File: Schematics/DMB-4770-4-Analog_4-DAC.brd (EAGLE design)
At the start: 32.8 x 86.9 mm, 66 parts

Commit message: Ajout schemas pour carte 4 entrées analog et 4 sorties analog
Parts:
- E$42, E$44, E$47, E$48: value 100K -> 80K
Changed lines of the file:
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@@
 <attribute name="NAME" x="13.6525" y="10.795" size="1.27" layer="51" ratio="16" rot="R180"/>
 </element>
-<element name="E$42" library="divers" package="R0805" value="100K" x="11.7475" y="14.2875" smashed="yes">
+<element name="E$42" library="divers" package="R0805" value="80K" x="11.7475" y="14.2875" smashed="yes">
 <attribute name="VALUE" x="6.985" y="13.97" size="0.8128" layer="27" ratio="16"/>
 <attribute name="NAME" x="10.16" y="15.24" size="1.27" layer="25" ratio="16"/>
@@
 <attribute name="NAME" x="19.3675" y="12.3825" size="1.27" layer="51" ratio="16" rot="R180"/>
 </element>
-<element name="E$44" library="divers" package="R0805" value="100K" x="21.2725" y="13.97" smashed="yes">
+<element name="E$44" library="divers" package="R0805" value="80K" x="21.2725" y="13.97" smashed="yes">
 <attribute name="VALUE" x="20.0025" y="12.065" size="0.8128" layer="27" ratio="16"/>
 <attribute name="NAME" x="19.685" y="14.9225" size="1.27" layer="25" ratio="16"/>
@@
 <attribute name="NAME" x="18.0975" y="26.9875" size="1.27" layer="51" ratio="16"/>
 </element>
-<element name="E$47" library="divers" package="R0805" value="100K" x="23.8125" y="25.4" smashed="yes">
+<element name="E$47" library="divers" package="R0805" value="80K" x="23.8125" y="25.4" smashed="yes">
 <attribute name="VALUE" x="22.5425" y="26.3525" size="0.8128" layer="27" ratio="16"/>
 <attribute name="NAME" x="22.225" y="26.3525" size="1.27" layer="25" ratio="16"/>
 <attribute name="NAME" x="21.9075" y="26.9875" size="1.27" layer="51" ratio="16"/>
 </element>
-<element name="E$48" library="divers" package="R0805" value="100K" x="11.7475" y="25.4" smashed="yes">
+<element name="E$48" library="divers" package="R0805" value="80K" x="11.7475" y="25.4" smashed="yes">
 <attribute name="VALUE" x="10.4775" y="26.3525" size="0.8128" layer="27" ratio="16"/>
 <attribute name="NAME" x="10.16" y="26.3525" size="1.27" layer="25" ratio="16"/>

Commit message: Correction valeurs
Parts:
- E$11, E$12, E$14, E$15, E$27, E$28, E$33, E$34: value 120K -> 102K
- E$41, E$43, E$45, E$46: value 20K -> 82.5K
- E$42, E$44, E$47, E$48: value 80K -> 330K
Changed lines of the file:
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@@
 <attribute name="NAME" x="26.8288" y="48.1806" size="1.27" layer="51" ratio="16" rot="R270"/>
 </element>
-<element name="E$11" library="divers" package="R0805" value="120K" x="27.305" y="50.165" smashed="yes" rot="R90">
+<element name="E$11" library="divers" package="R0805" value="102K" x="27.305" y="50.165" smashed="yes" rot="R90">
 <attribute name="VALUE" x="27.6225" y="52.07" size="0.8128" layer="27" ratio="16" rot="R90"/>
 <attribute name="NAME" x="26.3525" y="48.5775" size="1.27" layer="25" ratio="16" rot="R90"/>
 <attribute name="NAME" x="25.7175" y="48.26" size="1.27" layer="51" ratio="16" rot="R90"/>
 </element>
-<element name="E$12" library="divers" package="R0805" value="120K" x="27.305" y="46.0375" smashed="yes" rot="R270">
+<element name="E$12" library="divers" package="R0805" value="102K" x="27.305" y="46.0375" smashed="yes" rot="R270">
 <attribute name="VALUE" x="26.9875" y="44.1325" size="0.8128" layer="27" ratio="16" rot="R270"/>
 <attribute name="NAME" x="28.2575" y="47.625" size="1.27" layer="25" ratio="16" rot="R270"/>
@@
 <attribute name="NAME" x="22.6219" y="60.4838" size="1.27" layer="51" ratio="16"/>
 </element>
-<element name="E$14" library="divers" package="R0805" value="120K" x="20.6375" y="60.96" smashed="yes" rot="R180">
+<element name="E$14" library="divers" package="R0805" value="102K" x="20.6375" y="60.96" smashed="yes" rot="R180">
 <attribute name="VALUE" x="21.9075" y="62.865" size="0.8128" layer="27" ratio="16" rot="R180"/>
 <attribute name="NAME" x="22.225" y="60.0075" size="1.27" layer="25" ratio="16" rot="R180"/>
 <attribute name="NAME" x="22.5425" y="59.3725" size="1.27" layer="51" ratio="16" rot="R180"/>
 </element>
-<element name="E$15" library="divers" package="R0805" value="120K" x="24.765" y="60.96" smashed="yes">
+<element name="E$15" library="divers" package="R0805" value="102K" x="24.765" y="60.96" smashed="yes">
 <attribute name="VALUE" x="23.8125" y="61.9125" size="0.8128" layer="27" ratio="16"/>
 <attribute name="NAME" x="23.1775" y="61.9125" size="1.27" layer="25" ratio="16"/>
@@
 <attribute name="NAME" x="10.2394" y="60.4838" size="1.27" layer="51" ratio="16"/>
 </element>
-<element name="E$27" library="divers" package="R0805" value="120K" x="8.255" y="60.96" smashed="yes" rot="R180">
+<element name="E$27" library="divers" package="R0805" value="102K" x="8.255" y="60.96" smashed="yes" rot="R180">
 <attribute name="VALUE" x="9.8425" y="62.865" size="0.8128" layer="27" ratio="16" rot="R180"/>
 <attribute name="NAME" x="9.8425" y="60.0075" size="1.27" layer="25" ratio="16" rot="R180"/>
 <attribute name="NAME" x="10.16" y="59.3725" size="1.27" layer="51" ratio="16" rot="R180"/>
 </element>
-<element name="E$28" library="divers" package="R0805" value="120K" x="12.3825" y="60.96" smashed="yes">
+<element name="E$28" library="divers" package="R0805" value="102K" x="12.3825" y="60.96" smashed="yes">
 <attribute name="VALUE" x="13.97" y="62.865" size="0.8128" layer="27" ratio="16" rot="R180"/>
 <attribute name="NAME" x="10.795" y="61.9125" size="1.27" layer="25" ratio="16"/>
@@
 <attribute name="NAME" x="5.8737" y="48.0219" size="1.27" layer="51" ratio="16" rot="R90"/>
 </element>
-<element name="E$33" library="divers" package="R0805" value="120K" x="4.7625" y="46.0375" smashed="yes" rot="R270">
+<element name="E$33" library="divers" package="R0805" value="102K" x="4.7625" y="46.0375" smashed="yes" rot="R270">
 <attribute name="VALUE" x="4.445" y="44.1325" size="0.8128" layer="27" ratio="16" rot="R270"/>
 <attribute name="NAME" x="5.715" y="47.625" size="1.27" layer="25" ratio="16" rot="R270"/>
 <attribute name="NAME" x="6.35" y="47.9425" size="1.27" layer="51" ratio="16" rot="R270"/>
 </element>
-<element name="E$34" library="divers" package="R0805" value="120K" x="4.7625" y="50.165" smashed="yes" rot="R90">
+<element name="E$34" library="divers" package="R0805" value="102K" x="4.7625" y="50.165" smashed="yes" rot="R90">
 <attribute name="VALUE" x="5.08" y="52.07" size="0.8128" layer="27" ratio="16" rot="R90"/>
 <attribute name="NAME" x="3.81" y="48.5775" size="1.27" layer="25" ratio="16" rot="R90"/>
@@
 </element>
 <element name="E$40" library="SparkFun-AnalogIC" package="SOIC-14" value="OPA4171" x="18.415" y="19.685"/>
-<element name="E$41" library="divers" package="R0805" value="20K" x="11.7475" y="12.3825" smashed="yes" rot="R180">
+<element name="E$41" library="divers" package="R0805" value="82.5K" x="11.7475" y="12.3825" smashed="yes" rot="R180">
 <attribute name="VALUE" x="13.0175" y="11.1125" size="0.8128" layer="27" ratio="16" rot="R180"/>
 <attribute name="NAME" x="13.335" y="11.43" size="1.27" layer="25" ratio="16" rot="R180"/>
 <attribute name="NAME" x="13.6525" y="10.795" size="1.27" layer="51" ratio="16" rot="R180"/>
 </element>
-<element name="E$42" library="divers" package="R0805" value="80K" x="11.7475" y="14.2875" smashed="yes">
+<element name="E$42" library="divers" package="R0805" value="330K" x="11.7475" y="14.2875" smashed="yes">
 <attribute name="VALUE" x="6.985" y="13.97" size="0.8128" layer="27" ratio="16"/>
 <attribute name="NAME" x="10.16" y="15.24" size="1.27" layer="25" ratio="16"/>
 <attribute name="NAME" x="9.8425" y="15.875" size="1.27" layer="51" ratio="16"/>
 </element>
-<element name="E$43" library="divers" package="R0805" value="20K" x="17.4625" y="13.97" smashed="yes" rot="R180">
+<element name="E$43" library="divers" package="R0805" value="82.5K" x="17.4625" y="13.97" smashed="yes" rot="R180">
 <attribute name="VALUE" x="16.51" y="12.065" size="0.8128" layer="27" ratio="16"/>
 <attribute name="NAME" x="19.05" y="13.0175" size="1.27" layer="25" ratio="16" rot="R180"/>
 <attribute name="NAME" x="19.3675" y="12.3825" size="1.27" layer="51" ratio="16" rot="R180"/>
 </element>
-<element name="E$44" library="divers" package="R0805" value="80K" x="21.2725" y="13.97" smashed="yes">
+<element name="E$44" library="divers" package="R0805" value="330K" x="21.2725" y="13.97" smashed="yes">
 <attribute name="VALUE" x="20.0025" y="12.065" size="0.8128" layer="27" ratio="16"/>
 <attribute name="NAME" x="19.685" y="14.9225" size="1.27" layer="25" ratio="16"/>
 <attribute name="NAME" x="19.3675" y="15.5575" size="1.27" layer="51" ratio="16"/>
 </element>
-<element name="E$45" library="divers" package="R0805" value="20K" x="15.5575" y="25.4" smashed="yes" rot="R180">
+<element name="E$45" library="divers" package="R0805" value="82.5K" x="15.5575" y="25.4" smashed="yes" rot="R180">
 <attribute name="VALUE" x="14.605" y="26.3525" size="0.8128" layer="27" ratio="16"/>
 <attribute name="NAME" x="17.145" y="24.4475" size="1.27" layer="25" ratio="16" rot="R180"/>
 <attribute name="NAME" x="17.4625" y="23.8125" size="1.27" layer="51" ratio="16" rot="R180"/>
 </element>
-<element name="E$46" library="divers" package="R0805" value="20K" x="20.0025" y="25.4" smashed="yes">
+<element name="E$46" library="divers" package="R0805" value="82.5K" x="20.0025" y="25.4" smashed="yes">
 <attribute name="VALUE" x="19.05" y="26.3525" size="0.8128" layer="27" ratio="16"/>
 <attribute name="NAME" x="18.415" y="26.3525" size="1.27" layer="25" ratio="16"/>
 <attribute name="NAME" x="18.0975" y="26.9875" size="1.27" layer="51" ratio="16"/>
 </element>
-<element name="E$47" library="divers" package="R0805" value="80K" x="23.8125" y="25.4" smashed="yes">
+<element name="E$47" library="divers" package="R0805" value="330K" x="23.8125" y="25.4" smashed="yes">
 <attribute name="VALUE" x="22.5425" y="26.3525" size="0.8128" layer="27" ratio="16"/>
 <attribute name="NAME" x="22.225" y="26.3525" size="1.27" layer="25" ratio="16"/>
 <attribute name="NAME" x="21.9075" y="26.9875" size="1.27" layer="51" ratio="16"/>
 </element>
-<element name="E$48" library="divers" package="R0805" value="80K" x="11.7475" y="25.4" smashed="yes">
+<element name="E$48" library="divers" package="R0805" value="330K" x="11.7475" y="25.4" smashed="yes">
 <attribute name="VALUE" x="10.4775" y="26.3525" size="0.8128" layer="27" ratio="16"/>
 <attribute name="NAME" x="10.16" y="26.3525" size="1.27" layer="25" ratio="16"/>

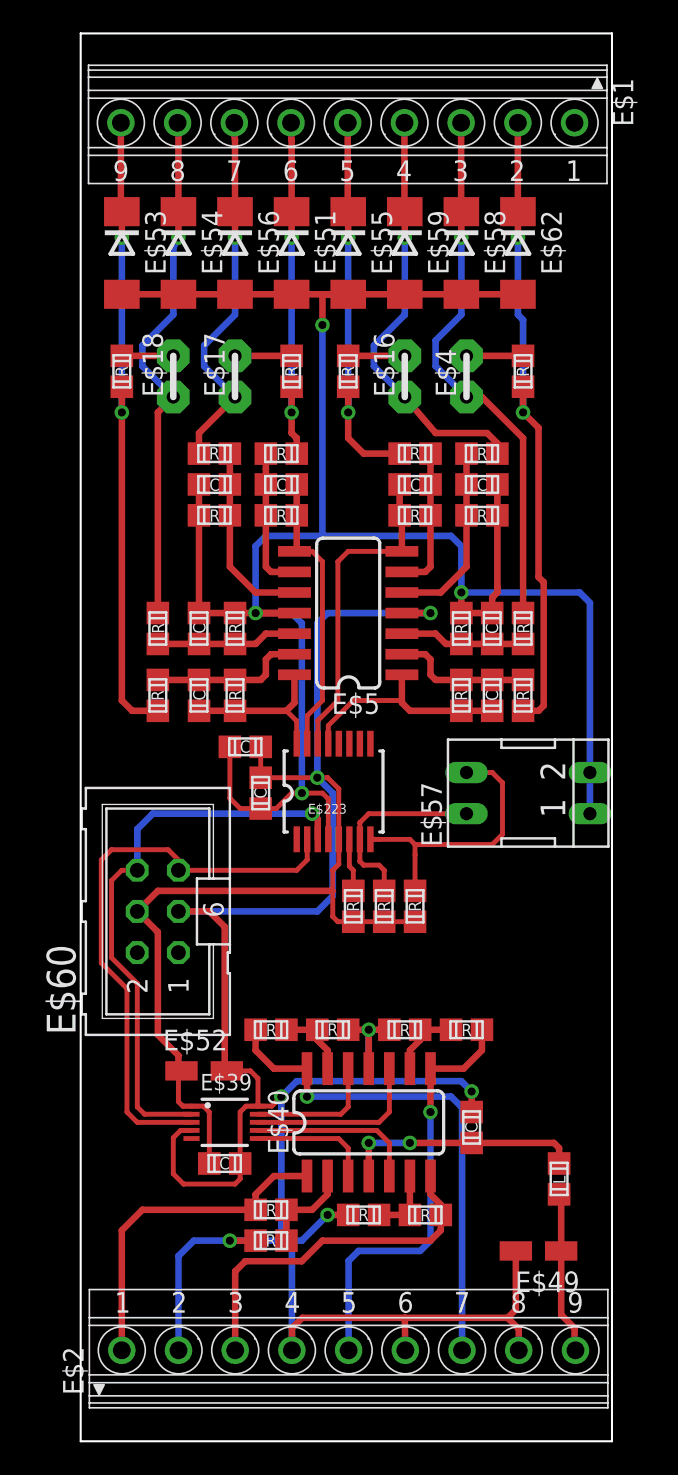
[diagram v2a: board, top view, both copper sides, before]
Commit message: Correction Resistance Sense 0-20mA
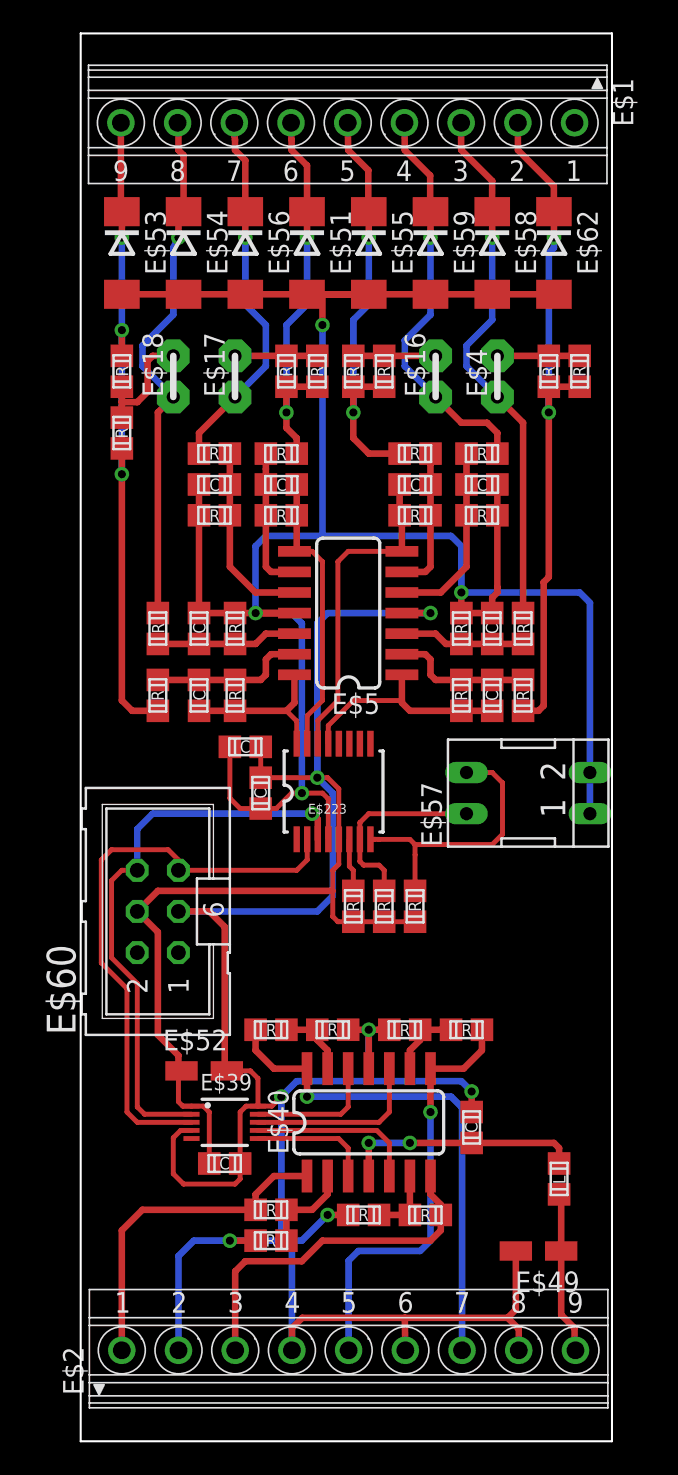
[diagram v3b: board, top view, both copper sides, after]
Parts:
- added E$63, E$64, E$65, E$66: 500, divers:R0805
- moved E$20 3.81 mm to (2.54, 62.2)
- moved E$62 2.22 mm to (29.2, 73.3)
- moved E$4 1.91 mm to (25.7, 65.7)
- moved E$16 1.90 mm to (21.9, 65.7)
- moved E$58 1.90 mm to (25.4, 73.3)
- moved E$59 1.59 mm to (21.6, 73.3)
- moved E$7 1.59 mm to (28.9, 66.0)
- moved E$55 1.27 mm to (17.8, 73.3)
- moved E$51 0.95 mm to (14.0, 73.3)
- moved E$56 0.63 mm to (10.2, 73.3)
- moved E$19 0.32 mm to (12.7, 66.0)
- moved E$54 0.32 mm to (6.35, 73.3)
- moved E$8 0.32 mm to (16.8, 66.0)
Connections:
- net IN1-: now also E$66.2
- net IN2-: now also E$65.2
- net IN3-: now also E$64.2
- net IN4-: now also E$63.2
- net S$10: now also E$63.1
- net S$15: now also E$66.1
- net S$20: now also E$65.1
- net S$21: now also E$64.1
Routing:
- net S$15: track 3.18 -> 7.38 mm
- net GND: track 334.4 -> 337.9 mm
- net IN2-: track 22.1 -> 25.1 mm
- net IN3-: track 24.6 -> 27.1 mm
- net IN4-: track 39.6 -> 42.1 mm
- net S$20: track 3.49 -> 5.08 mm
- net S$10: track 3.49 -> 5.08 mm
- net IN1-: track 39.8 -> 41.3 mm, vias 2 -> 3
- net S$21: track 3.49 -> 5.08 mm
- net IN3+: track 26.1 -> 25.0 mm
- net IN4+: track 33.7 -> 33.2 mm

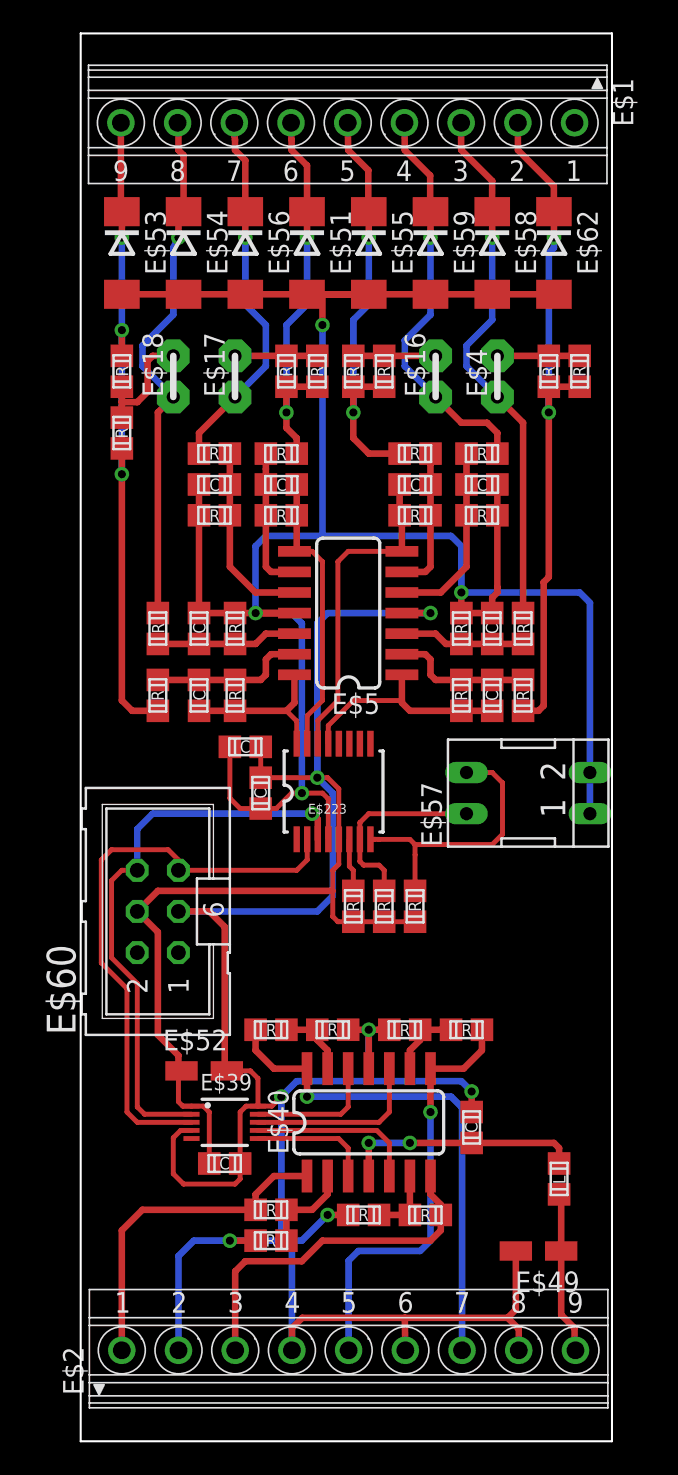
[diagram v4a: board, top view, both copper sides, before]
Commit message: Correction erreur GND
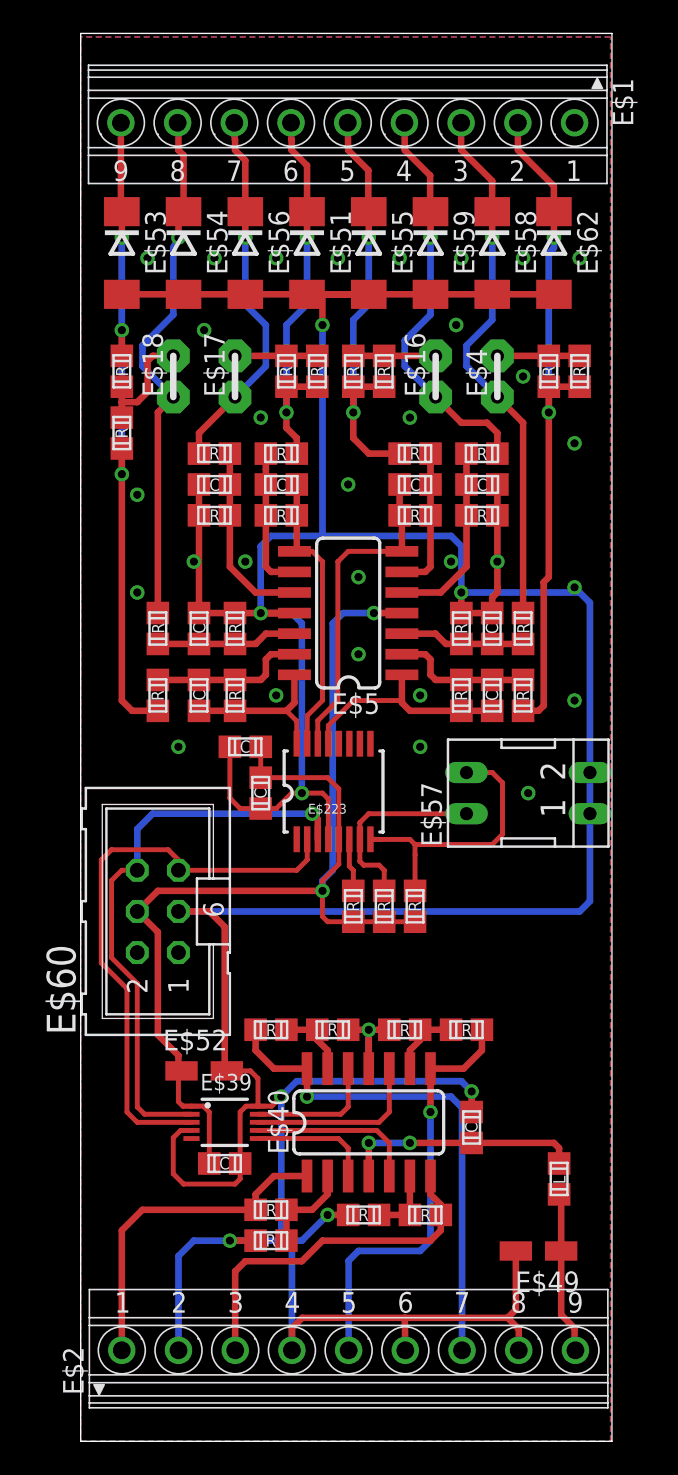
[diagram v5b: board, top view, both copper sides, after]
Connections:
- new net 3V3: E$223.5, E$224.2, E$225.2, E$226.2, E$3.2, E$37.1, E$39.1, E$5.4, E$50.1, E$52.+, E$60.4
- net GND: no longer E$223.5, E$224.2, E$225.2, E$226.2, E$3.2, E$37.1, E$39.1, E$5.4, E$50.1, E$52.+, E$60.4
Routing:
- net 3V3: track 0.00 -> 72.7 mm, vias 0 -> 2
- net GND: track 337.9 -> 280.7 mm, vias 11 -> 39
- added copper zone on layer 1, net GND
- added copper zone on layer 16, net GND

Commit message: Modifications plan de masse et routage
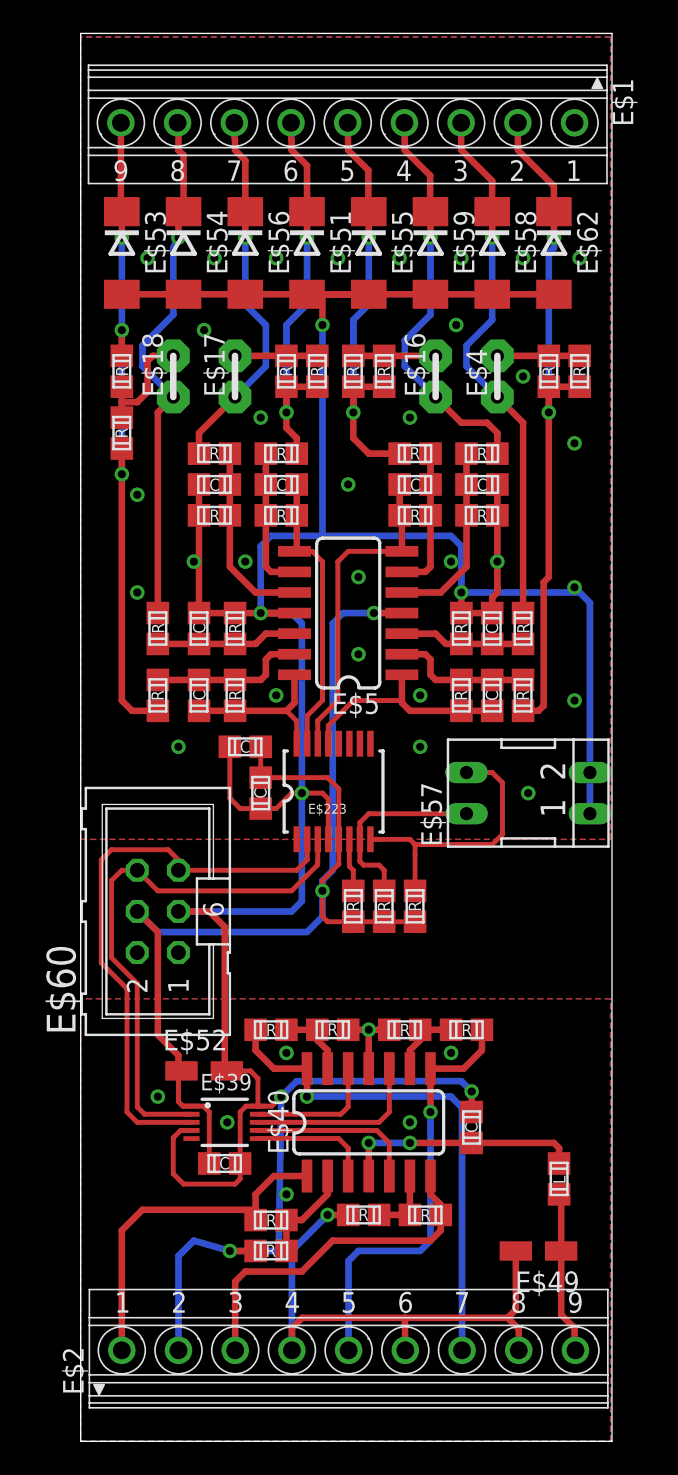
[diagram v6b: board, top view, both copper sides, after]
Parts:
- moved E$41 0.63 mm to (11.7, 11.7)
- moved E$42 0.63 mm to (11.7, 13.7)
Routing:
- net GND: track 280.7 -> 264.6 mm, vias 39 -> 45
- net 3V3: track 72.7 -> 74.7 mm
- net SCL: track 35.5 -> 33.9 mm, vias 1 -> 0
- net S$38: track 20.8 -> 22.1 mm
